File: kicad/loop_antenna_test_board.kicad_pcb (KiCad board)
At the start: 2 copper layers, 59.7 x 27.9 mm, 5 parts

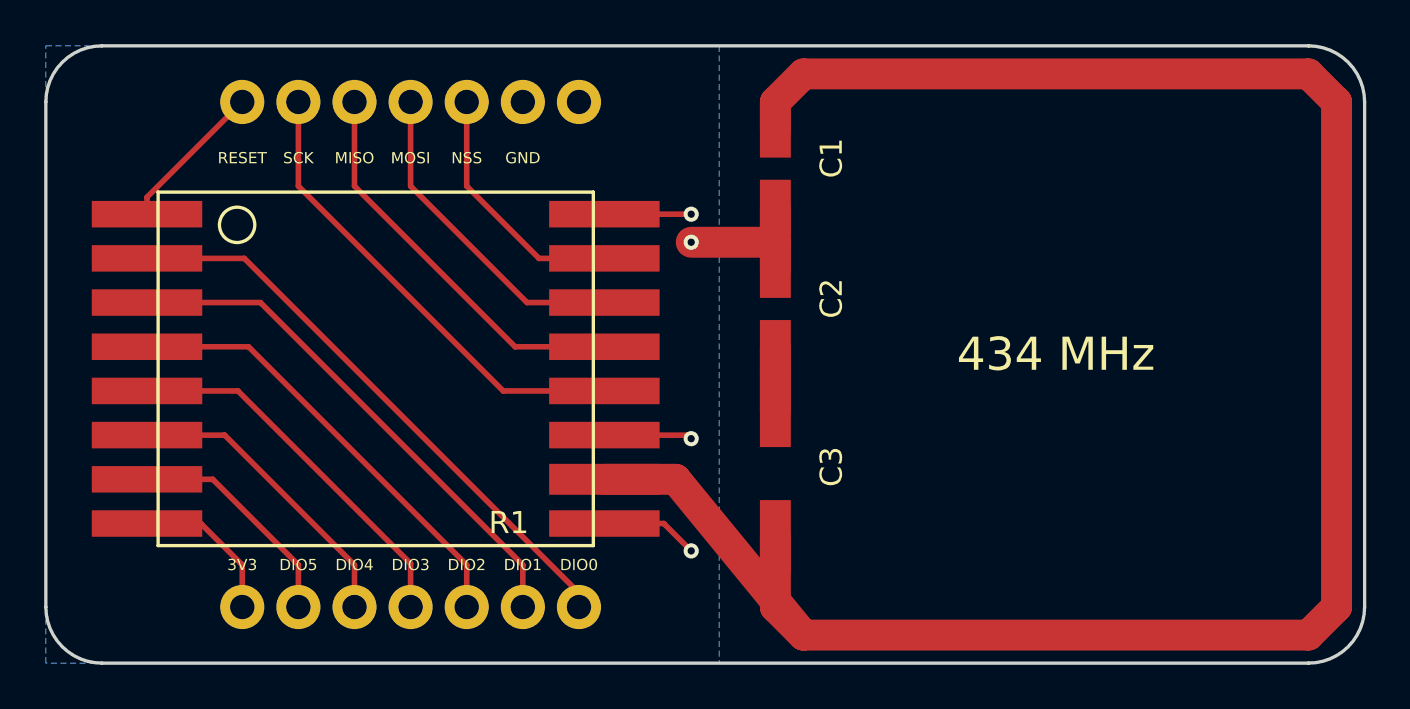
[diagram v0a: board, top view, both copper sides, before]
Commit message: smoothed antenna feed
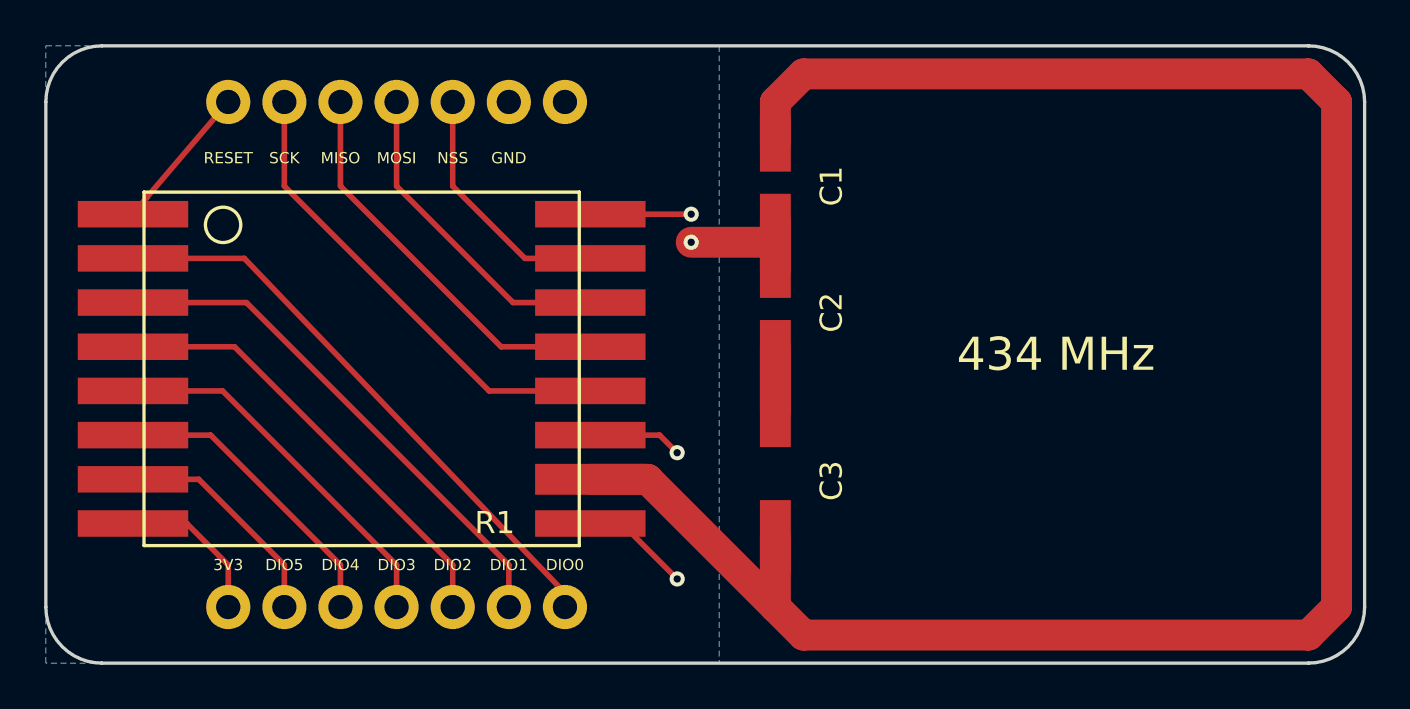
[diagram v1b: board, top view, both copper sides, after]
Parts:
- moved R1 0.64 mm to (131.4, 108.0)
- moved C1 0.64 mm to (160.0, 104.8)
- moved R2 0.63 mm to (142.9, 115.6)
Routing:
- net Net-(R1-Pad15): track 11.4 -> 13.7 mm
- net Net-(C1-Pad1): track 92.6 -> 91.6 mm
- net GND: track 19.0 -> 19.8 mm

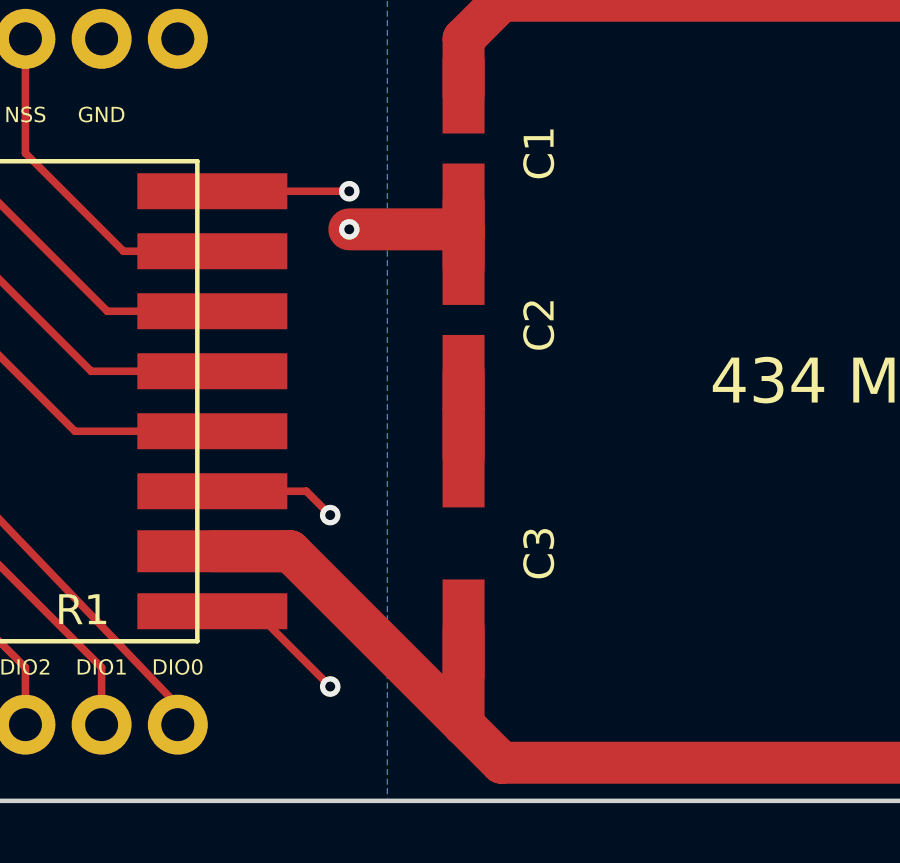
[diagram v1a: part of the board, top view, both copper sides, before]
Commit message: switched to only having two positions for capacitors in the antenna
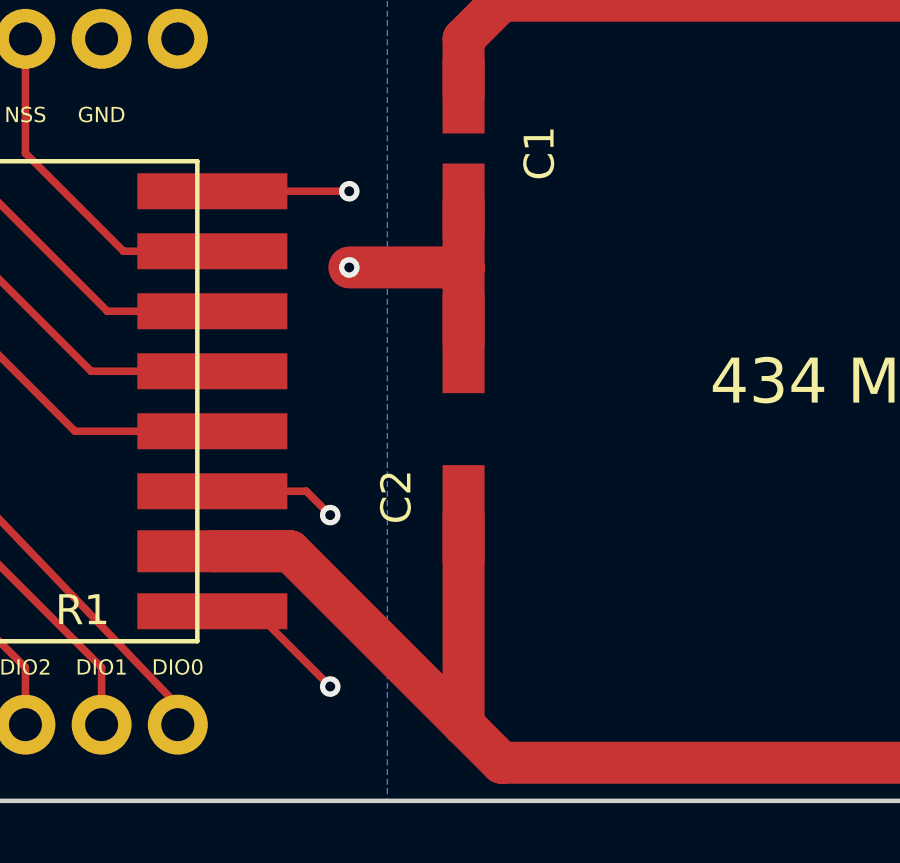
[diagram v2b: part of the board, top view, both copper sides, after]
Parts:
- removed C3: CTRIM, loop_antenna_test_board:CAP_TUNABLE
- C2: value C -> CTRIM; footprint loop_antenna_test_board:CAP -> loop_antenna_test_board:CAP_TUNABLE
- moved C2 2.54 mm to (160.0, 113.0)
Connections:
- C2 pad 2: Net-(C2-Pad2) -> Net-(C1-Pad1)
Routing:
- net Net-(C1-Pad1): track 91.6 -> 95.4 mm
- net Net-(C2-Pad2): track 2.85 -> 0.00 mm
- net GND: track 19.8 -> 22.4 mm

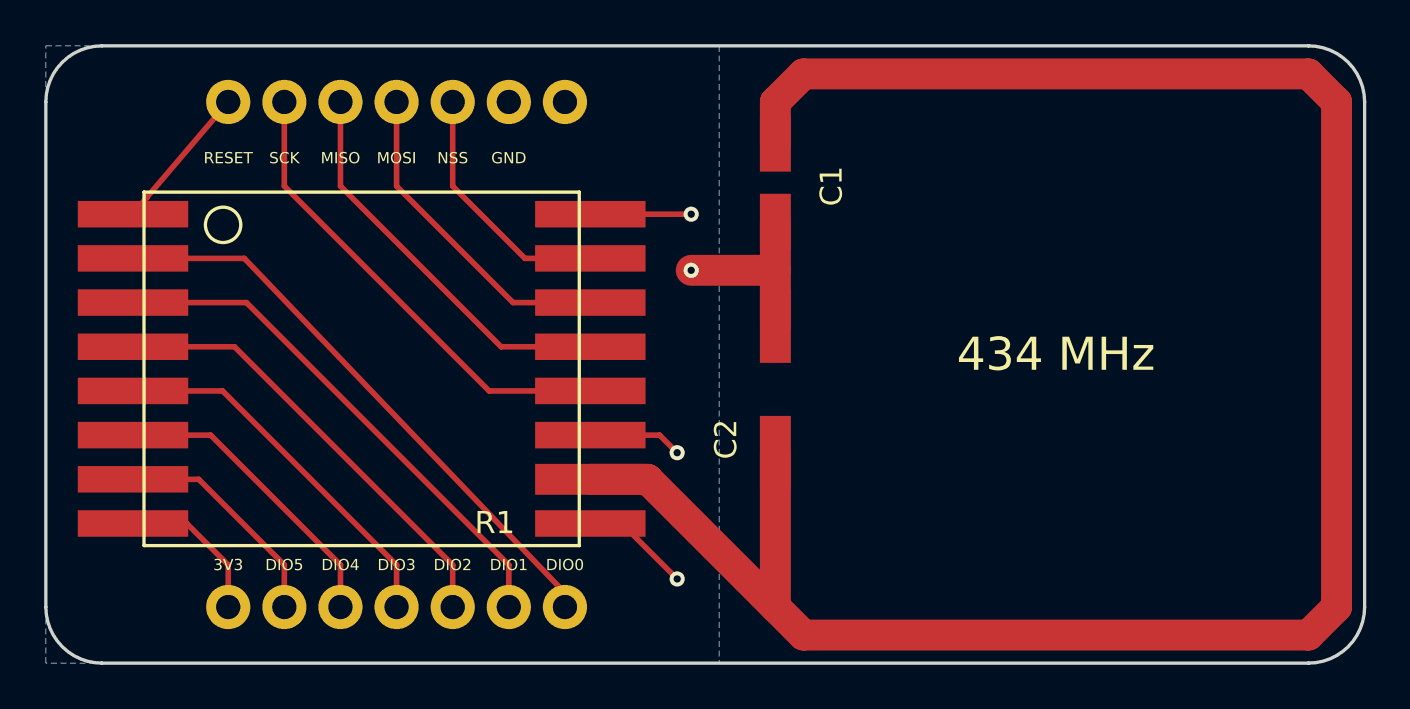
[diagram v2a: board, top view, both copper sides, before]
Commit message: reduced the size of the board to match it to the components
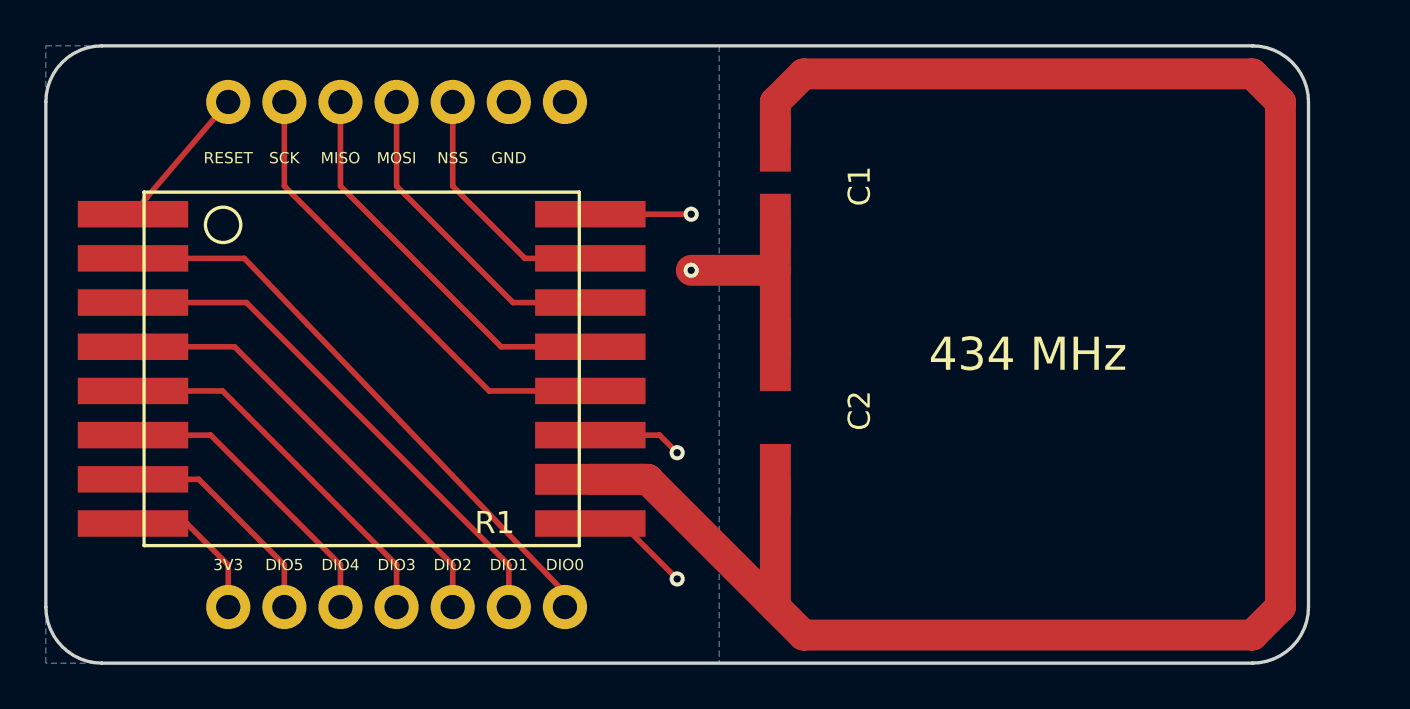
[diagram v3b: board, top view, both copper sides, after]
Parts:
- moved C2 1.27 mm to (160.0, 114.3)
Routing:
- net Net-(C1-Pad1): track 95.4 -> 89.1 mm
- net GND: track 22.4 -> 23.6 mm
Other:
- board size 59.7 x 27.9 mm -> 57.2 x 27.9 mm
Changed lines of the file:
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@@
     (links 19)
     (no_connects 0)
-    (area 126.924999 100.254999 186.765001 128.345001)
+    (area 126.924999 100.254999 186.765001 131.1024)
     (thickness 1.6)
     (drawings 24)
@@
     (0 F.Cu signal)
     (31 B.Cu signal)
-    (36 B.SilkS user hide)
-    (37 F.SilkS user hide)
+    (36 B.SilkS user)
+    (37 F.SilkS user)
     (38 B.Mask user)
     (39 F.Mask user)
@@
   )
   (setup
-    (last_trace_width 1.4)
+    (last_trace_width 0.254)
     (user_trace_width 1.4)
     (trace_clearance 0.1524)
@@
   (module CAP (layer F.Cu)
     (at 160.02 104.775 270)
-    (fp_text reference C1 (at 1.905 -2.54 270) (layer F.SilkS)
+    (fp_text reference C1 (at 1.905 -3.81 270) (layer F.SilkS)
       (effects (font (size 1 1) (thickness 0.15)))
     )
@@
   )
   (module loop_antenna_test_board:CAP_TUNABLE (layer F.Cu)
-    (at 160.02 113.03 270)
-    (fp_text reference C2 (at 5.1054 2.2352 270) (layer F.SilkS)
+    (at 160.02 114.3 270)
+    (fp_text reference C2 (at 2.54 -3.81 270) (layer F.SilkS)
       (effects (font (size 1 1) (thickness 0.15)))
     )
@@
       (net 1 "Net-(C1-Pad1)"))
   )
+  (gr_line (start 184.15 125.73) (end 184.15 102.87) (angle 90) (layer Edge.Cuts) (width 0.15))
+  (gr_arc (start 181.61 125.73) (end 184.15 125.73) (angle 90) (layer Edge.Cuts) (width 0.15))
+  (gr_arc (start 181.61 102.87) (end 181.61 100.33) (angle 90) (layer Edge.Cuts) (width 0.15))
   (gr_text RESET (at 135.255 105.41) (layer F.SilkS)
     (effects (font (size 0.508 0.508) (thickness 0.127)))
@@
   )
   (gr_arc (start 129.54 102.87) (end 127 102.87) (angle 90) (layer Edge.Cuts) (width 0.15))
-  (gr_arc (start 184.15 102.87) (end 184.15 100.33) (angle 90) (layer Edge.Cuts) (width 0.15))
-  (gr_arc (start 184.15 125.73) (end 186.69 125.73) (angle 90) (layer Edge.Cuts) (width 0.15))
   (gr_arc (start 129.54 125.73) (end 129.54 128.27) (angle 90) (layer Edge.Cuts) (width 0.15))
-  (gr_line (start 186.69 125.73) (end 186.69 102.87) (angle 90) (layer Edge.Cuts) (width 0.15))
-  (gr_line (start 129.54 128.27) (end 184.15 128.27) (angle 90) (layer Edge.Cuts) (width 0.15))
+  (gr_line (start 129.54 128.27) (end 181.61 128.27) (angle 90) (layer Edge.Cuts) (width 0.15))
   (gr_line (start 127 102.87) (end 127 125.73) (angle 90) (layer Edge.Cuts) (width 0.15))
-  (gr_line (start 184.15 100.33) (end 129.54 100.33) (angle 90) (layer Edge.Cuts) (width 0.15))
-  (gr_text "LOOP ANTENNA TEST BOARD\nV 1.0.0" (at 158.75 114.3) (layer B.SilkS)
+  (gr_line (start 181.61 100.33) (end 129.54 100.33) (angle 90) (layer Edge.Cuts) (width 0.15))
+  (gr_text "LOOP ANTENNA TEST BOARD\nV 1.0.0" (at 157.48 114.3) (layer B.SilkS)
     (effects (font (size 1.5 1.5) (thickness 0.3)) (justify mirror))
   )
-  (gr_text hochreiner.net (at 157.48 125.73) (layer B.SilkS)
+  (gr_text hochreiner.net (at 156.21 125.73) (layer B.SilkS)
     (effects (font (size 1.5 1.5) (thickness 0.3)) (justify mirror))
   )
-  (gr_text "434 MHz" (at 172.72 114.3) (layer F.SilkS)
+  (gr_text "434 MHz" (at 171.45 114.3) (layer F.SilkS)
     (effects (font (size 1.5 1.5) (thickness 0.3)))
   )
   (segment (start 151.645 119.95) (end 154.24 119.95) (width 1.4) (layer F.Cu) (net 1))
   (segment (start 154.24 119.95) (end 160.02 125.73) (width 1.4) (layer F.Cu) (net 1))
-  (segment (start 161.29 101.6) (end 184.15 101.6) (width 1.4) (layer F.Cu) (net 1))
-  (segment (start 184.15 101.6) (end 185.42 102.87) (width 1.4) (layer F.Cu) (net 1))
-  (segment (start 185.42 102.87) (end 185.42 125.73) (width 1.4) (layer F.Cu) (net 1))
-  (segment (start 185.42 125.73) (end 184.15 127) (width 1.4) (layer F.Cu) (net 1))
+  (segment (start 161.29 101.6) (end 181.61 101.6) (width 1.4) (layer F.Cu) (net 1))
+  (segment (start 181.61 101.6) (end 182.88 102.87) (width 1.4) (layer F.Cu) (net 1))
+  (segment (start 182.88 102.87) (end 182.88 125.73) (width 1.4) (layer F.Cu) (net 1))
+  (segment (start 182.88 125.73) (end 181.61 127) (width 1.4) (layer F.Cu) (net 1))
   (segment (start 160.02 104.775) (end 160.02 102.87) (width 1.4) (layer F.Cu) (net 1) (status 10))
   (segment (start 160.02 102.87) (end 161.29 101.6) (width 1.4) (layer F.Cu) (net 1))
-  (segment (start 160.02 125.73) (end 160.02 118.73) (width 1.4) (layer F.Cu) (net 1) (status 20))
-  (segment (start 184.15 127) (end 161.29 127) (width 1.4) (layer F.Cu) (net 1))
+  (segment (start 160.02 125.73) (end 160.02 120) (width 1.4) (layer F.Cu) (net 1) (status 20))
+  (segment (start 181.61 127) (end 161.29 127) (width 1.4) (layer F.Cu) (net 1))
   (segment (start 161.29 127) (end 160.02 125.73) (width 1.4) (layer F.Cu) (net 1))
   (segment (start 160.02 108.275) (end 160.02 110.49) (width 1.4) (layer F.Cu) (net 2))
-  (segment (start 160.02 113.03) (end 160.02 110.49) (width 1.4) (layer F.Cu) (net 2))
+  (segment (start 160.02 114.3) (end 160.02 110.49) (width 1.4) (layer F.Cu) (net 2) (status 10))
   (via (at 156.21 110.49) (size 0.6858) (drill 0.3302) (layers F.Cu B.Cu) (net 2))
   (segment (start 160.02 110.49) (end 156.21 110.49) (width 1.4) (layer F.Cu) (net 2))
